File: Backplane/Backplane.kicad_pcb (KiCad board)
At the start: 2 copper layers, 76 x 164 mm, 21 parts, among them J1 Front panel, J2 System bus

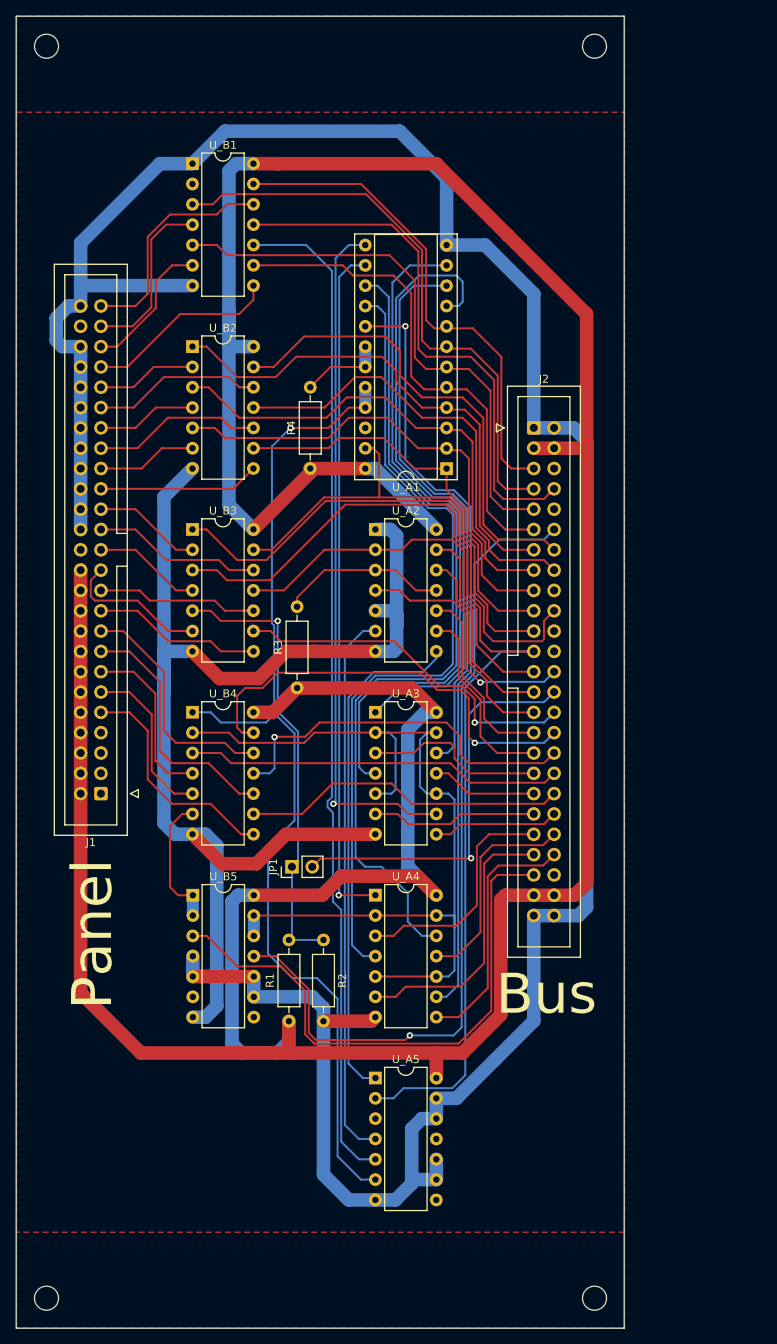
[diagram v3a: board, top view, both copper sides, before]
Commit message: Backplane: Fix RA15 signal
Original schematic by Nakazoto contained an error, which has been fixed. So no
need for an experimental jumper on RA15 line; and 220-330 divider actually sits
on a Reset signal, coming from the front panel.
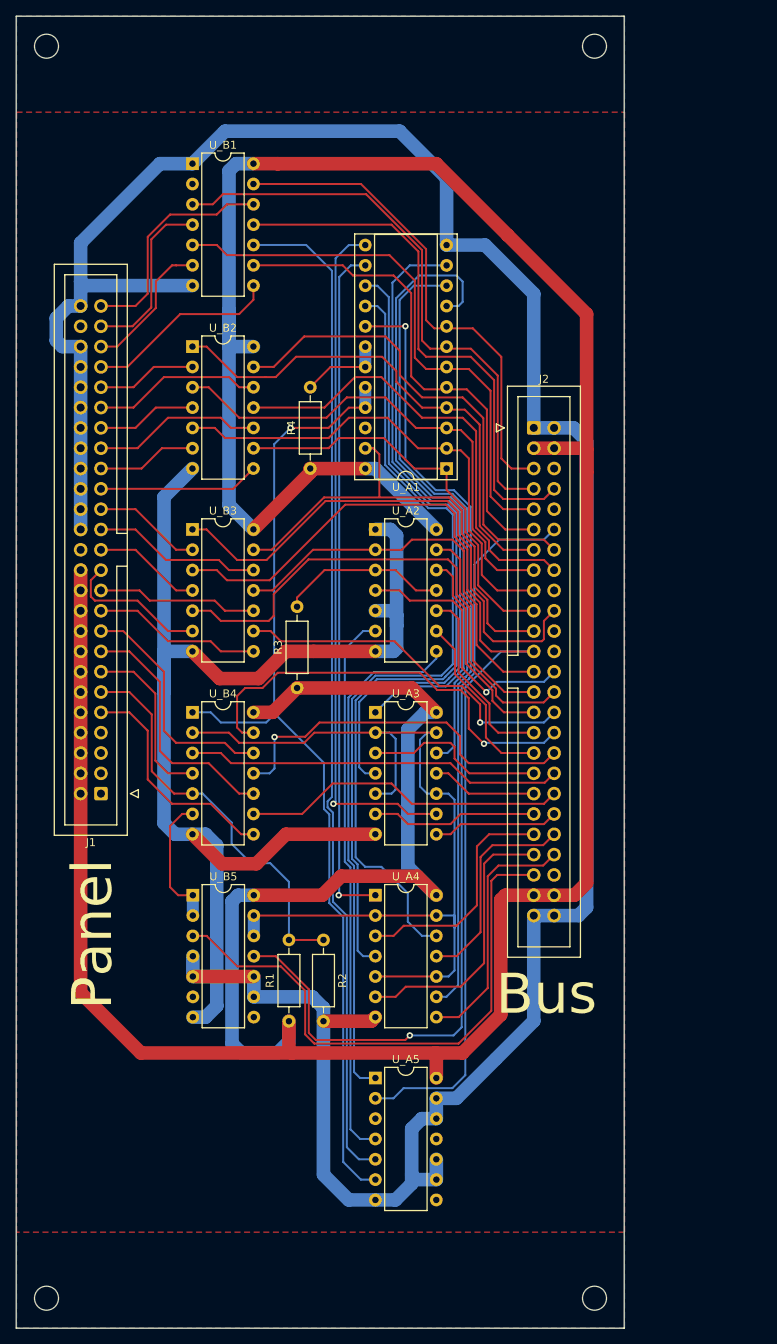
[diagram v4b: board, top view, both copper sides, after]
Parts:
- removed JP1: Experimental, Connector_PinHeader_2.54mm:PinHeader_1x02_P2.54mm_Vertical
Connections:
- net Gnd renamed GND
- net Vcc renamed +5V
- R1 pad 2: Net-(JP1-Pad1) -> /~{ResetOut}
- R2 pad 1: Net-(JP1-Pad1) -> /~{ResetOut}
- U_B3 pad 5: Net-(JP1-Pad1) -> /Sys.~{RA_{15}}
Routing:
- net Net-(JP1-Pad1): track 56.9 -> 0.00 mm, vias 1 -> 0
- net /~{ResetOut}: track 20.9 -> 50.6 mm
- net /Sys.~{RA_{15}}: track 50.2 -> 64.9 mm, vias 1 -> 0
- net Net-(U_A1-Pad20): track 130.1 -> 125.3 mm
- net /Sys.~{CA_{15}}: track 24.0 -> 22.7 mm
- net /Sys.~{PA_{11}}: track 31.6 -> 32.9 mm
- net /Sys.~{CPL_{1}}: track 54.1 -> 53.5 mm

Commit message: Backplane: Modular design
Make sure that a horizontal bus connector can be installed, thus extending this
shortened backplane PCB to a full size, if PCB-mounted edge slots can be
purchased.
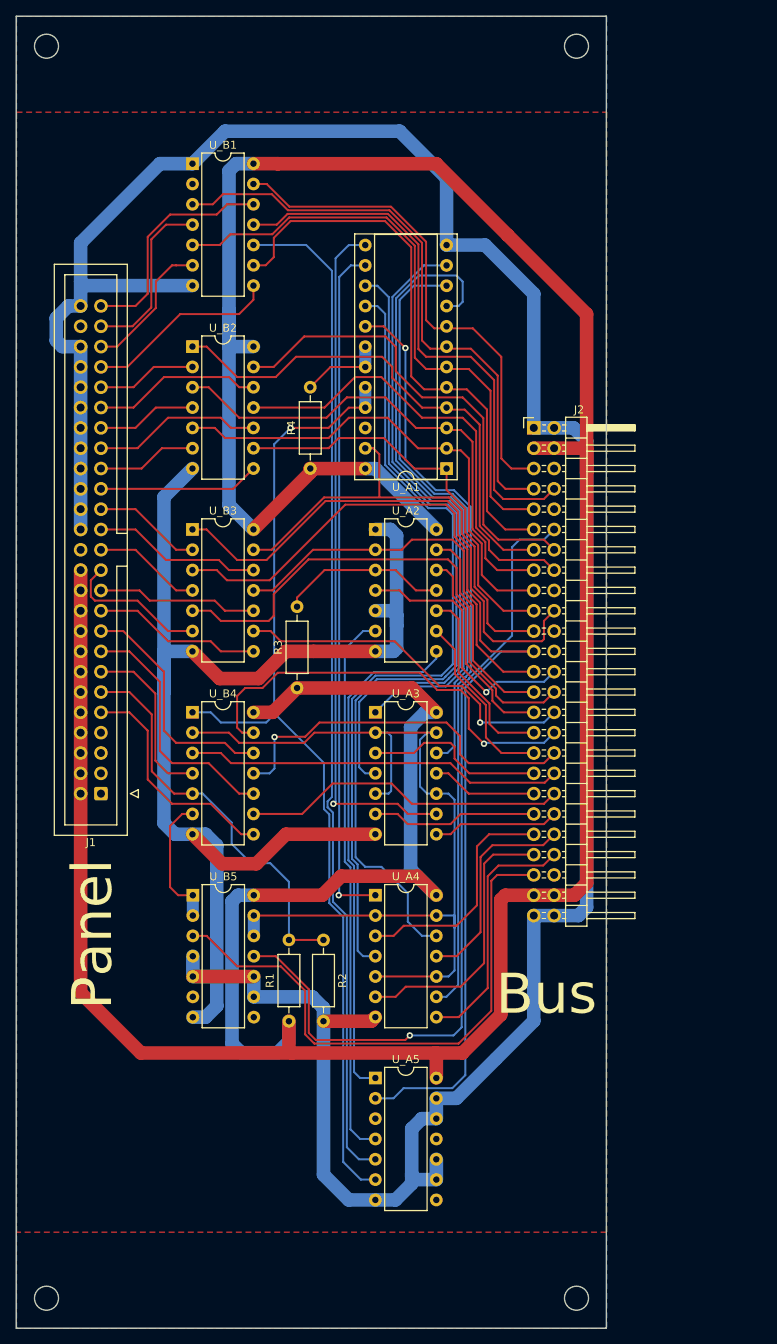
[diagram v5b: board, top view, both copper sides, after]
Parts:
- J2: footprint Connector_IDC:IDC-Header_2x25_P2.54mm_Vertical -> Connector_PinHeader_2.54mm:PinHeader_2x25_P2.54mm_Horizontal
- moved REF** 2.25 mm to (139.5, 181.2)
- moved REF** 2.25 mm to (139.5, 24.8)
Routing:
- net /Sys.~{A_{3}}: track 62.3 -> 71.6 mm
- net /Sys.~{A_{2}}: track 69.7 -> 75.1 mm
- net /Sys.~{RDIN}: track 67.5 -> 69.1 mm
- net Net-(U_A1-Pad17): track 96.1 -> 94.5 mm
- net /Sys.~{DRDY}: track 104.5 -> 103.0 mm
- net Net-(U_A1-Pad11): track 85.4 -> 84.4 mm
- net Net-(U_A3-Pad10): track 117.4 -> 116.6 mm
- net /Sys.~{A_{0}}: track 62.4 -> 63.0 mm
- net /Sys.~{A_{1}}: track 72.8 -> 73.3 mm
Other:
- board size 76 x 164 mm -> 73.8 x 164 mm

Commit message: Backplane: Erratum E001
Incorrect U_A1 chip width
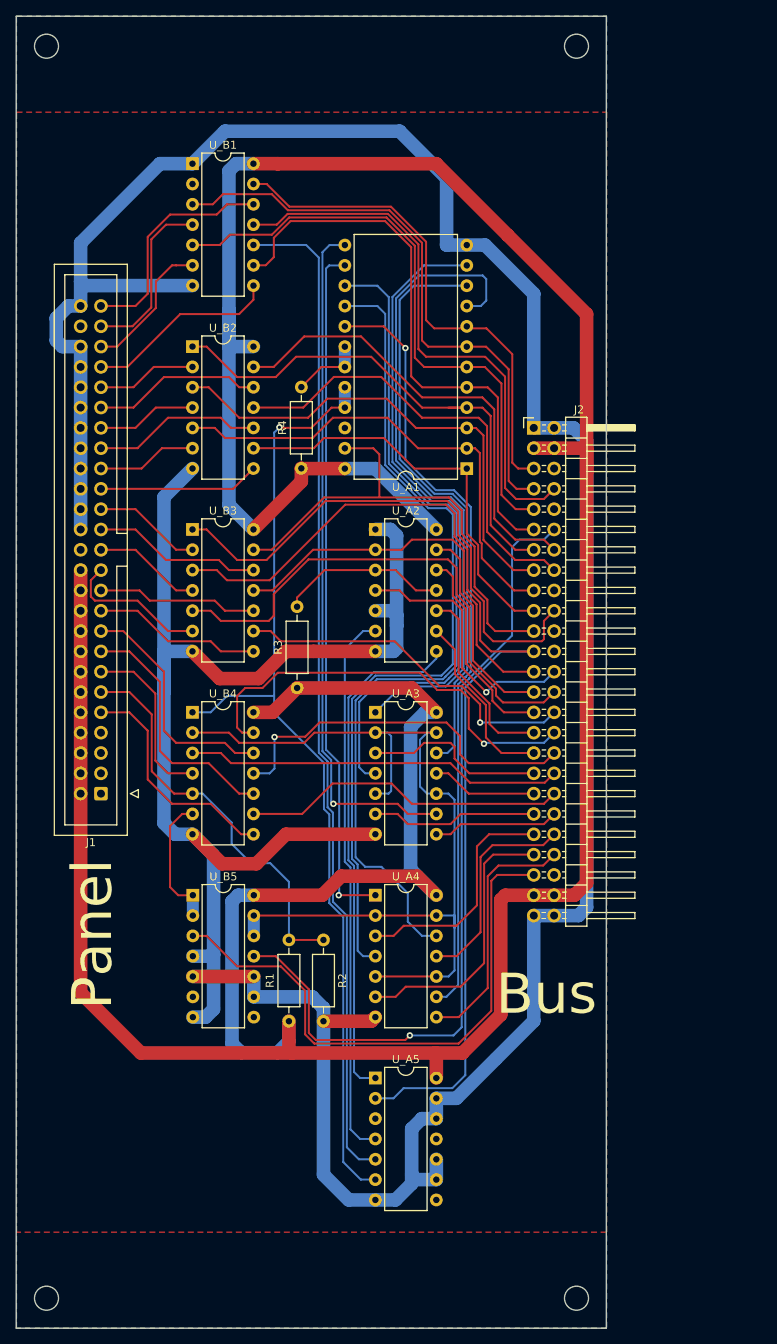
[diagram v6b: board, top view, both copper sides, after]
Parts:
- U_A1: footprint Package_DIP:DIP-24_W10.16mm_Socket -> Package_DIP:DIP-24_W15.24mm
- moved U_A1 2.52 mm to (125.8, 77.5)
- moved R4 1.11 mm to (105.1, 77.5)
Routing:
- net Net-(U_A1-Pad9): track 79.0 -> 82.5 mm
- net Net-(U_A1-Pad15): track 104.7 -> 107.2 mm
- net Net-(U_A1-Pad17): track 94.5 -> 97.0 mm
- net Net-(U_A1-Pad16): track 100.2 -> 102.7 mm
- net /Sys.~{A_{8}}: track 58.5 -> 61.0 mm
- net Net-(U_A1-Pad11): track 84.4 -> 86.9 mm
- net Net-(U_A1-Pad10): track 70.5 -> 73.0 mm
- net /Sys.~{A_{4}}: track 63.4 -> 65.6 mm
- net GND: track 495.6 -> 493.7 mm
- net /Sys.~{RA_{14}}: track 59.8 -> 58.2 mm
- net Net-(R4-Pad2): track 10.5 -> 9.02 mm
- net Net-(U_A1-Pad20): track 125.3 -> 124.0 mm
- net /Sys.~{A_{3}}: track 71.6 -> 72.5 mm
- net +5V: track 468.5 -> 469.2 mm
- net /Sys.~{A_{7}}: track 50.8 -> 51.4 mm
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
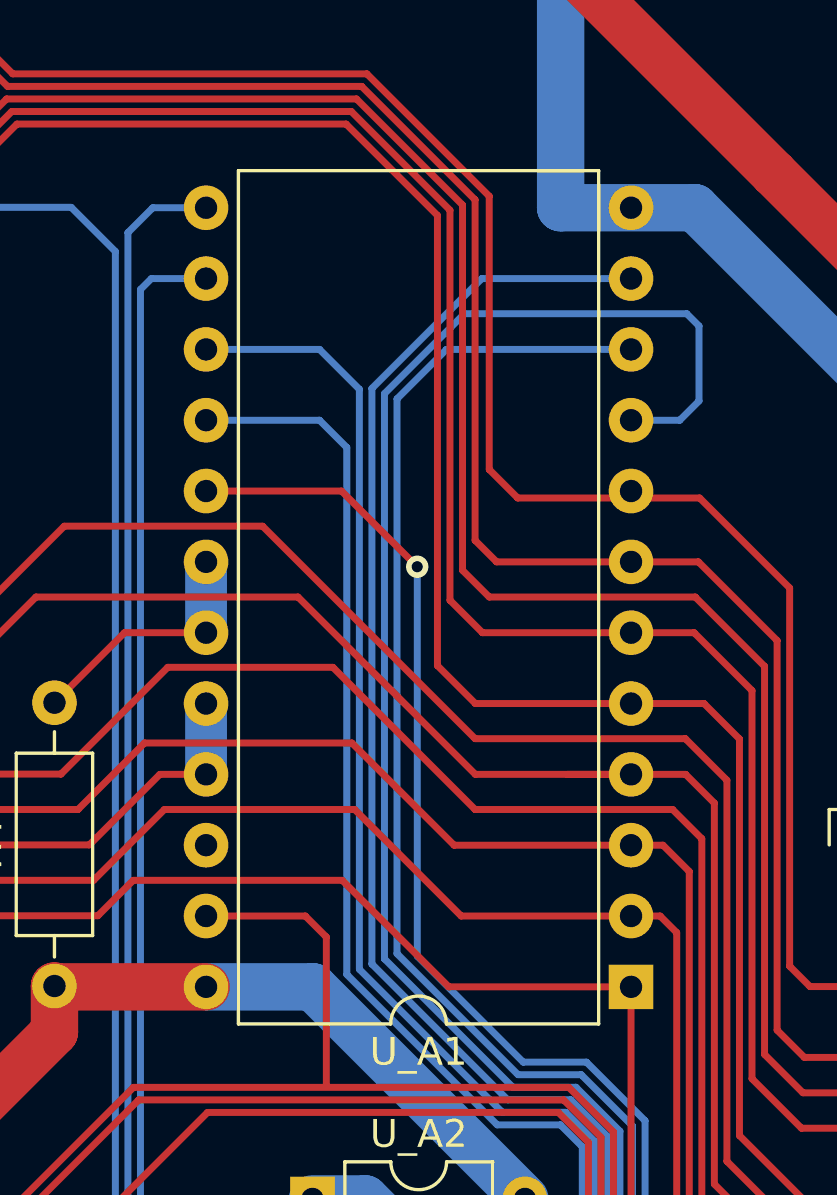
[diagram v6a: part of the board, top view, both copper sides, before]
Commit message: Backplane: Use socket for U_A1
Just for compliance, let's change U_A1 footprint to socket
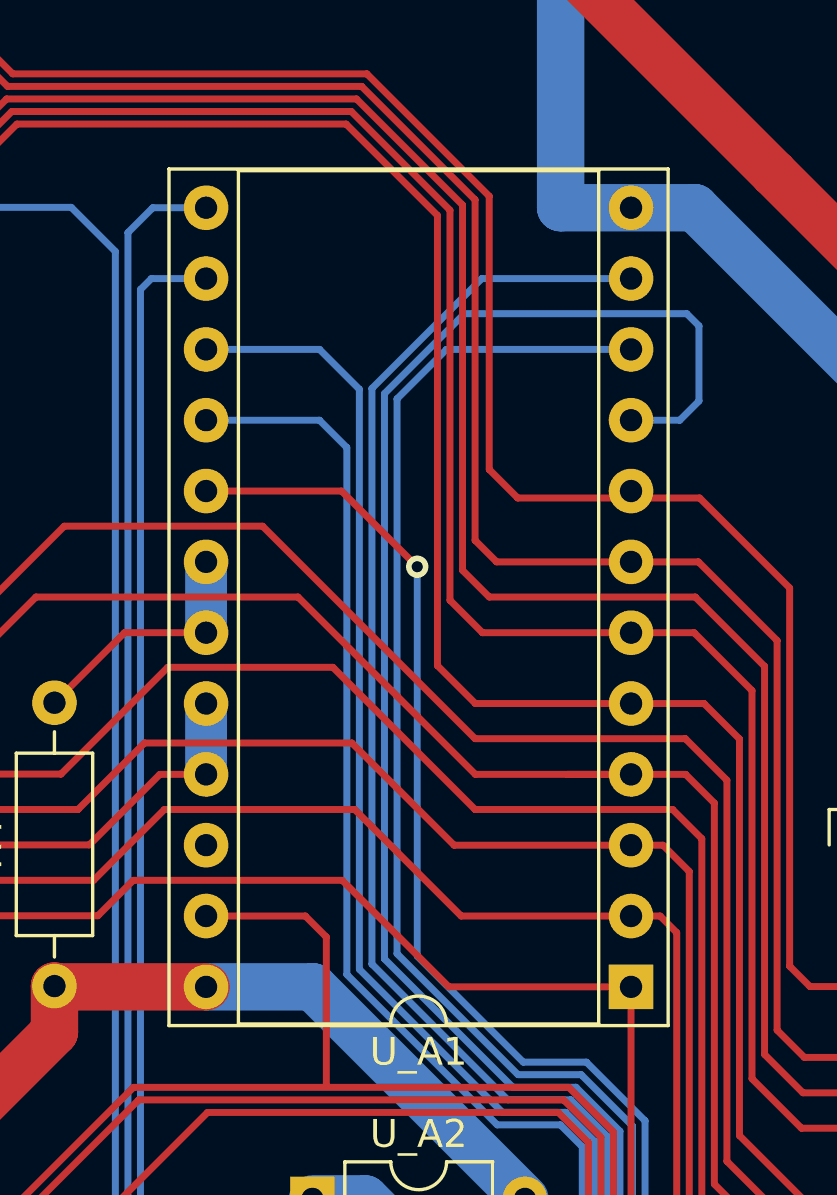
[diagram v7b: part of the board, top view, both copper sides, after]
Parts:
- U_A1: footprint Package_DIP:DIP-24_W15.24mm -> Package_DIP:DIP-24_W15.24mm_Socket
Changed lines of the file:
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@@
     )
   )
-  (footprint "Package_DIP:DIP-24_W15.24mm" (layer "F.Cu")
+  (footprint "Package_DIP:DIP-24_W15.24mm_Socket" (layer "F.Cu")
     (at 125.782198 77.55 180)
-    (descr "24-lead though-hole mounted DIP package, row spacing 15.24 mm (600 mils)")
-    (tags "THT DIP DIL PDIP 2.54mm 15.24mm 600mil")
+    (descr "24-lead though-hole mounted DIP package, row spacing 15.24 mm (600 mils), Socket")
+    (tags "THT DIP DIL PDIP 2.54mm 15.24mm 600mil Socket")
     (property "Sheetfile" "Backplane.kicad_sch")
     (property "Sheetname" "")
@@
       (effects (font (size 1 1) (thickness 0.15)))
     )
+    (fp_line (start 14.08 29.27) (end 14.08 -1.33) (layer "F.SilkS") (width 0.12))
+    (fp_line (start -1.33 -1.39) (end -1.33 29.33) (layer "F.SilkS") (width 0.12))
+    (fp_line (start 1.16 29.27) (end 14.08 29.27) (layer "F.SilkS") (width 0.12))
+    (fp_line (start 1.16 -1.33) (end 1.16 29.27) (layer "F.SilkS") (width 0.12))
+    (fp_line (start 16.57 -1.39) (end -1.33 -1.39) (layer "F.SilkS") (width 0.12))
+    (fp_line (start 14.08 -1.33) (end 8.62 -1.33) (layer "F.SilkS") (width 0.12))
+    (fp_line (start 16.57 29.33) (end 16.57 -1.39) (layer "F.SilkS") (width 0.12))
     (fp_line (start 6.62 -1.33) (end 1.16 -1.33) (layer "F.SilkS") (width 0.12))
-    (fp_line (start 14.08 29.27) (end 14.08 -1.33) (layer "F.SilkS") (width 0.12))
-    (fp_line (start 1.16 -1.33) (end 1.16 29.27) (layer "F.SilkS") (width 0.12))
-    (fp_line (start 14.08 -1.33) (end 8.62 -1.33) (layer "F.SilkS") (width 0.12))
-    (fp_line (start 1.16 29.27) (end 14.08 29.27) (layer "F.SilkS") (width 0.12))
+    (fp_line (start -1.33 29.33) (end 16.57 29.33) (layer "F.SilkS") (width 0.12))
     (fp_arc (start 8.62 -1.33) (mid 7.62 -0.33) (end 6.62 -1.33) (layer "F.SilkS") (width 0.12))
-    (fp_line (start 16.3 29.5) (end 16.3 -1.55) (layer "F.CrtYd") (width 0.05))
-    (fp_line (start 16.3 -1.55) (end -1.05 -1.55) (layer "F.CrtYd") (width 0.05))
-    (fp_line (start -1.05 29.5) (end 16.3 29.5) (layer "F.CrtYd") (width 0.05))
-    (fp_line (start -1.05 -1.55) (end -1.05 29.5) (layer "F.CrtYd") (width 0.05))
-    (fp_line (start 14.985 29.21) (end 0.255 29.21) (layer "F.Fab") (width 0.1))
+    (fp_line (start -1.55 -1.6) (end -1.55 29.55) (layer "F.CrtYd") (width 0.05))
+    (fp_line (start 16.8 29.55) (end 16.8 -1.6) (layer "F.CrtYd") (width 0.05))
+    (fp_line (start -1.55 29.55) (end 16.8 29.55) (layer "F.CrtYd") (width 0.05))
+    (fp_line (start 16.8 -1.6) (end -1.55 -1.6) (layer "F.CrtYd") (width 0.05))
+    (fp_line (start 0.255 -0.27) (end 1.255 -1.27) (layer "F.Fab") (width 0.1))
+    (fp_line (start 0.255 29.21) (end 0.255 -0.27) (layer "F.Fab") (width 0.1))
+    (fp_line (start 16.51 29.27) (end 16.51 -1.33) (layer "F.Fab") (width 0.1))
     (fp_line (start 14.985 -1.27) (end 14.985 29.21) (layer "F.Fab") (width 0.1))
     (fp_line (start 1.255 -1.27) (end 14.985 -1.27) (layer "F.Fab") (width 0.1))
-    (fp_line (start 0.255 29.21) (end 0.255 -0.27) (layer "F.Fab") (width 0.1))
-    (fp_line (start 0.255 -0.27) (end 1.255 -1.27) (layer "F.Fab") (width 0.1))
+    (fp_line (start 14.985 29.21) (end 0.255 29.21) (layer "F.Fab") (width 0.1))
+    (fp_line (start -1.27 29.27) (end 16.51 29.27) (layer "F.Fab") (width 0.1))
+    (fp_line (start -1.27 -1.33) (end -1.27 29.27) (layer "F.Fab") (width 0.1))
+    (fp_line (start 16.51 -1.33) (end -1.27 -1.33) (layer "F.Fab") (width 0.1))
     (pad "1" thru_hole rect (at 0 0 180) (size 1.6 1.6) (drill 0.8) (layers *.Cu *.Mask)
       (net 3 "/Sys.~{A_{7}}") (pinfunction "A7") (pintype "input"))
@@
     (pad "24" thru_hole oval (at 15.24 0 180) (size 1.6 1.6) (drill 0.8) (layers *.Cu *.Mask)
       (net 90 "+5V") (pinfunction "VCC") (pintype "power_in"))
-    (model "${KICAD6_3DMODEL_DIR}/Package_DIP.3dshapes/DIP-24_W15.24mm.wrl"
+    (model "${KICAD6_3DMODEL_DIR}/Package_DIP.3dshapes/DIP-24_W15.24mm_Socket.wrl"
       (offset (xyz 0 0 0))
       (scale (xyz 1 1 1))

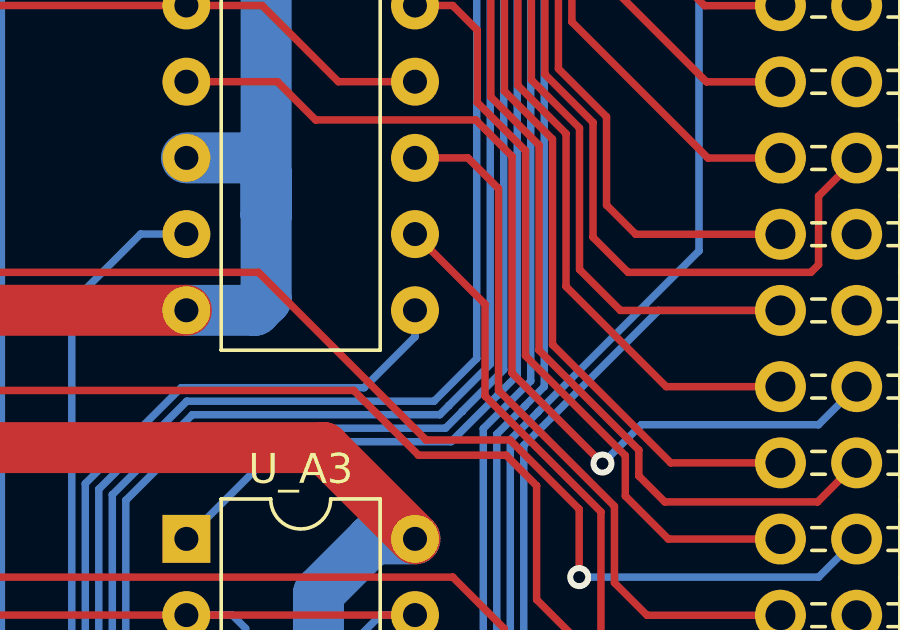
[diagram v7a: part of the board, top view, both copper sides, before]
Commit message: Some layout optimizations
Less vias
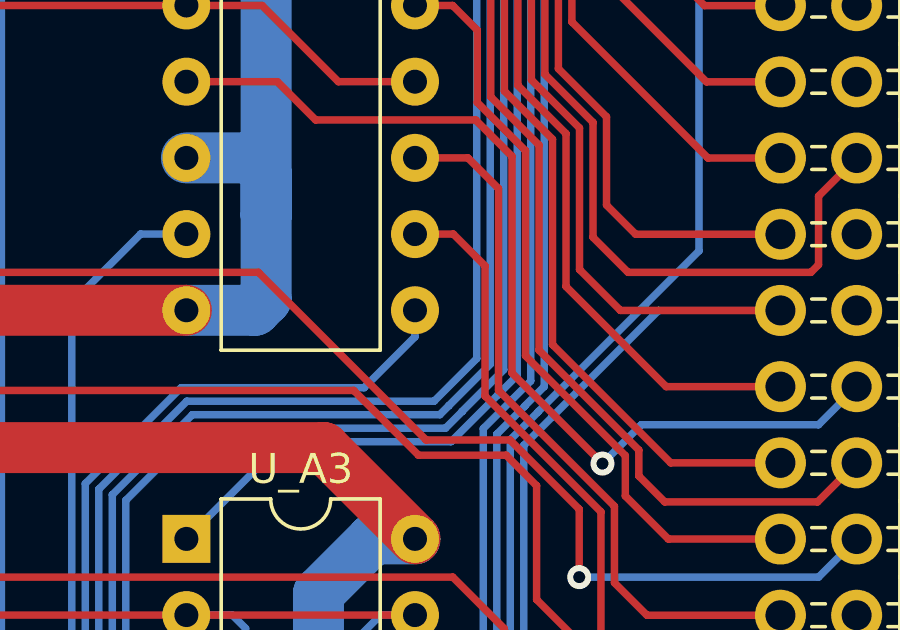
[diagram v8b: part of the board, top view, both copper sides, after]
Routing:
- net /Sys.~{CA_{15}}: track 22.7 -> 23.4 mm
